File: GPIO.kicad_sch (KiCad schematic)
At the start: 34 parts, among them J11 74LS245, J9 uPD446, K15 74LS04, U1 74LS245, U2 74LS10

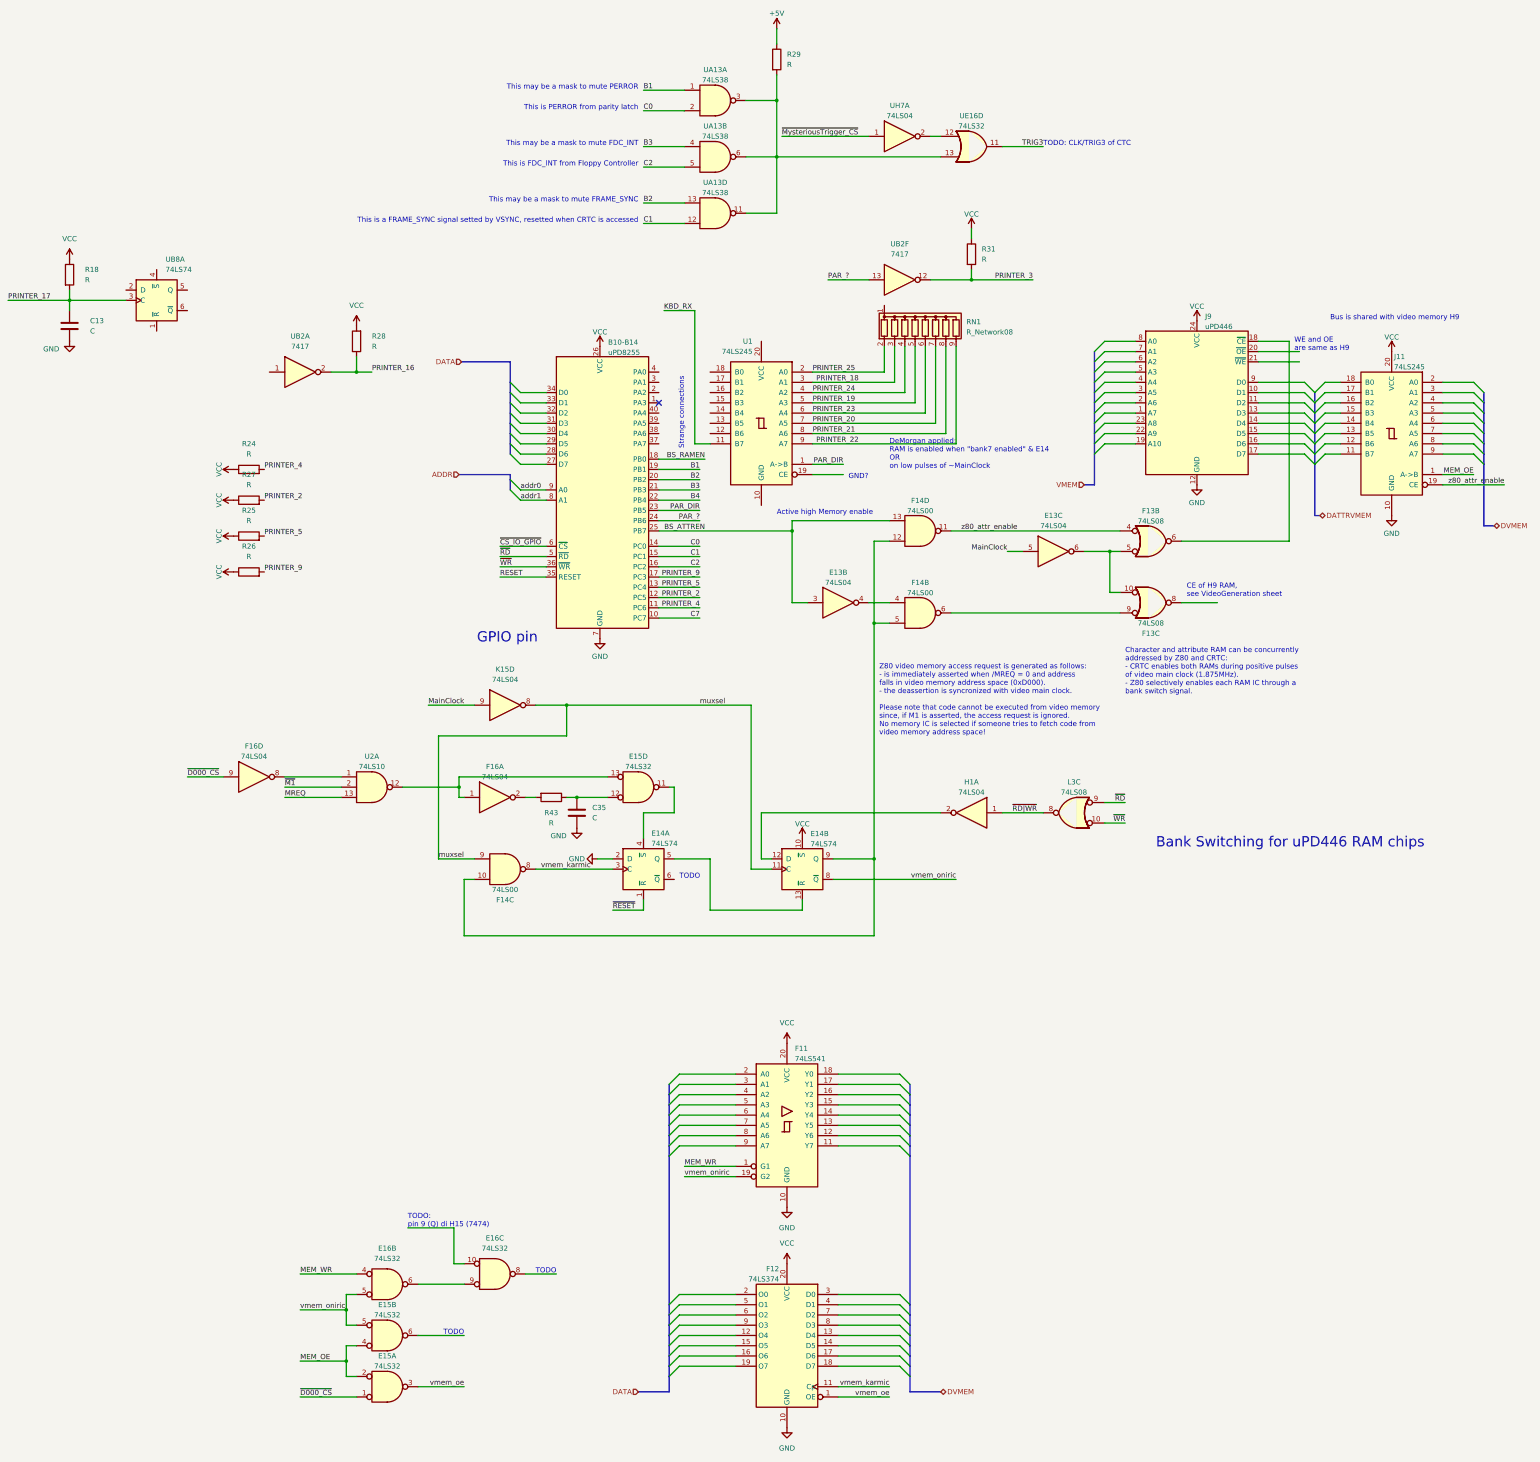
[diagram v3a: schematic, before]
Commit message: Discovered WE and OE signals for video memories, plus others
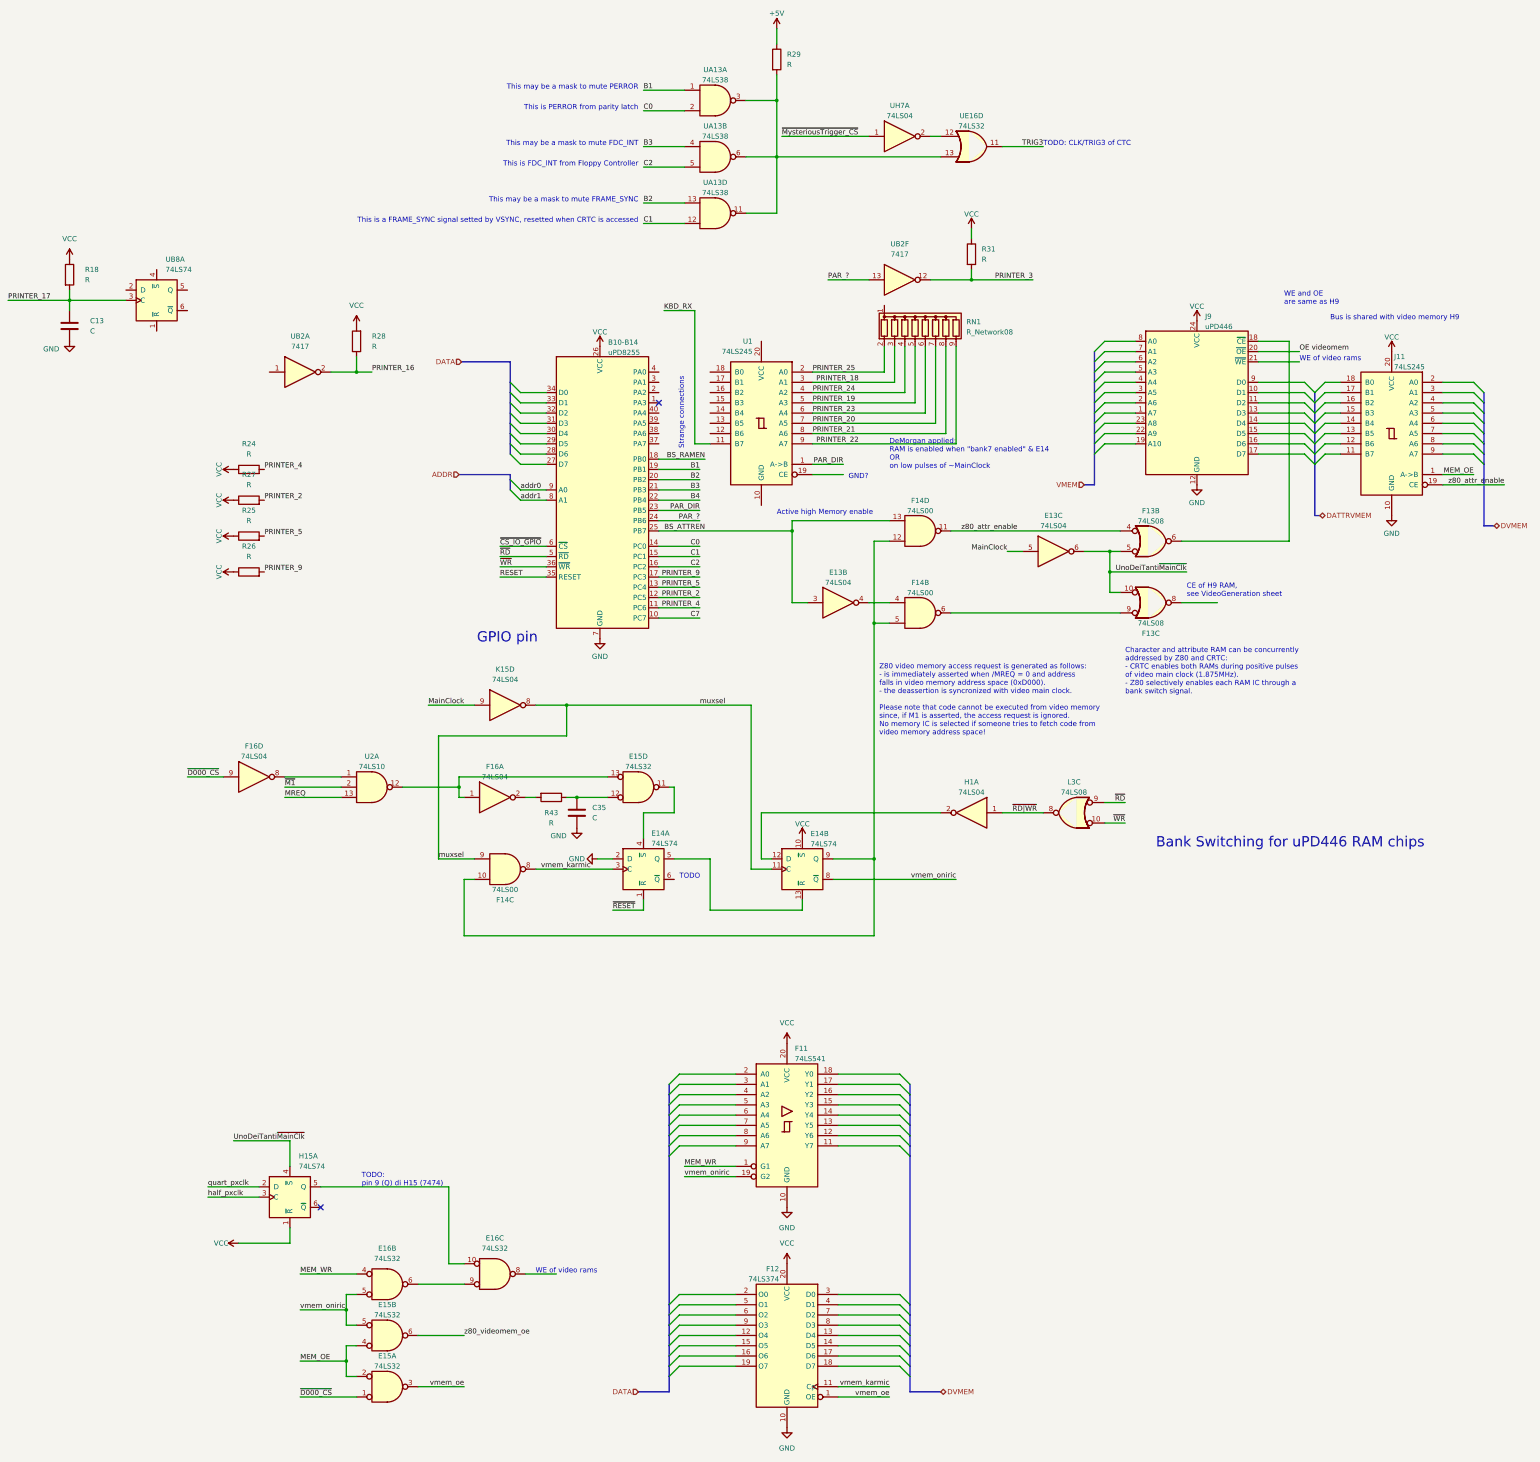
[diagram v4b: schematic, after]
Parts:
- added H15: 74LS74, symbol 74xx:74LS74
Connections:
- net VCC: now also H15.1 (~{R})
- net UnoDeiTanti~{MainClk}: now reaches E13.6, F13.10, F13.5
- net UnoDeiTanti~{MainClk}: now also H15.4 (~{S})
- net OE videomem: now reaches J9.20 (~{OE})
- net z80_videomem_oe: now reaches E15.6
- net at E16.10: now also H15.5 (Q)
- new net half_pxclk: H15.3 (C)
- new net quart_pxclk: H15.2 (D)
- no-connect marks 1 -> 2
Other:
- note added: "WE of video rams"
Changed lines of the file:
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@@
   (junction (at 49.53 147.32) (diameter 0) (color 0 0 0 0)
   )
+  (junction (at 181.61 91.44) (diameter 0) (color 0 0 0 0)
+  )
   (junction (at 20.32 144.78) (diameter 0) (color 0 0 0 0)
   )
@@
   )
   (no_connect (at 69.85 49.53))
+  (no_connect (at -13.97 248.92))
   (bus_entry (at 271.78 62.23) (size 2.54 2.54)
     (stroke (width 0) (type default))
@@
     (stroke (width 0) (type default))
   )
+  (wire (pts (xy -21.59 254) (xy -21.59 257.81))
+    (stroke (width 0) (type default))
+  )
   (wire (pts (xy 218.44 34.29) (xy 226.06 34.29))
     (stroke (width 0) (type default))
@@
     (stroke (width 0) (type default))
   )
-  (wire (pts (xy 19.05 262.89) (xy 19.05 254))
+  (wire (pts (xy 17.78 262.89) (xy 17.78 243.84))
     (stroke (width 0) (type default))
   )
@@
     (stroke (width 0) (type default))
   )
+  (wire (pts (xy -41.91 243.84) (xy -29.21 243.84))
+    (stroke (width 0) (type default))
+  )
   (wire (pts (xy 74.93 270.51) (xy 88.9 270.51))
     (stroke (width 0) (type default))
@@
     (stroke (width 0) (type default))
   )
+  (wire (pts (xy 200.66 91.44) (xy 181.61 91.44))
+    (stroke (width 0) (type default))
+  )
   (bus (pts (xy 274.32 62.23) (xy 274.32 64.77))
     (stroke (width 0) (type default))
@@
     (stroke (width 0) (type default))
   )
-  (wire (pts (xy 21.59 262.89) (xy 19.05 262.89))
+  (wire (pts (xy 17.78 262.89) (xy 21.59 262.89))
     (stroke (width 0) (type default))
   )
@@
     (stroke (width 0) (type default))
   )
+  (wire (pts (xy -13.97 243.84) (xy 17.78 243.84))
+    (stroke (width 0) (type default))
+  )
   (bus (pts (xy 177.8 57.15) (xy 177.8 59.69))
     (stroke (width 0) (type default))
@@
     (stroke (width 0) (type default))
   )
+  (wire (pts (xy 181.61 91.44) (xy 181.61 96.52))
+    (stroke (width 0) (type default))
+  )
   (wire (pts (xy 97.79 162.56) (xy 95.25 162.56))
     (stroke (width 0) (type default))
@@
     (stroke (width 0) (type default))
   )
+  (wire (pts (xy -34.29 257.81) (xy -21.59 257.81))
+    (stroke (width 0) (type default))
+  )
   (wire (pts (xy 114.3 231.14) (xy 129.54 231.14))
     (stroke (width 0) (type default))
@@
     (stroke (width 0) (type default))
   )
+  (wire (pts (xy -35.56 232.41) (xy -21.59 232.41))
+    (stroke (width 0) (type default))
+  )
   (wire (pts (xy 121.92 19.05) (xy 111.76 19.05))
     (stroke (width 0) (type default))
@@
     (stroke (width 0) (type default))
   )
-  (wire (pts (xy 181.61 86.36) (xy 181.61 96.52))
+  (wire (pts (xy 181.61 86.36) (xy 181.61 91.44))
     (stroke (width 0) (type default))
   )
@@
     (stroke (width 0) (type default))
   )
-  (wire (pts (xy 7.62 254) (xy 19.05 254))
-    (stroke (width 0) (type default))
-  )
   (bus (pts (xy 274.32 80.01) (xy 276.86 80.01))
     (stroke (width 0) (type default))
@@
     (stroke (width 0) (type default))
   )
+  (wire (pts (xy -41.91 246.38) (xy -29.21 246.38))
+    (stroke (width 0) (type default))
+  )
+  (wire (pts (xy -21.59 238.76) (xy -21.59 232.41))
+    (stroke (width 0) (type default))
+  )
   (wire (pts (xy 69.85 97.79) (xy 80.01 97.79))
     (stroke (width 0) (type default))
@@
     (effects (font (size 2.54 2.54)) (justify left bottom))
   )
-  (text "WE and OE\nare same as H9" (at 227.33 36.83 0)
+  (text "WE and OE\nare same as H9" (at 224.79 25.4 0)
     (effects (font (size 1.27 1.27)) (justify left bottom))
   )
@@
     (effects (font (size 1.27 1.27)) (justify left bottom))
   )
-  (text "TODO" (at 44.45 265.43 0)
+  (text "WE of video rams" (at 54.61 265.43 0)
     (effects (font (size 1.27 1.27)) (justify right bottom))
   )
+  (text "WE of video rams" (at 228.6 39.37 0)
+    (effects (font (size 1.27 1.27)) (justify left bottom))
+  )
   (text "Character and attribute RAM can be concurrently\naddressed by Z80 and CRTC:\n- CRTC enables both RAMs during positive pulses\nof video main clock (1.875MHz).\n- Z80 selectively enables each RAM IC through a\nbank switch signal."
     (at 185.42 121.92 0)
@@
     (effects (font (size 1.27 1.27)) (justify right bottom))
   )
-  (text "TODO:\npin 9 (Q) di H15 (7474)" (at 7.62 254 0)
+  (text "TODO:\npin 9 (Q) di H15 (7474)" (at -3.81 243.84 0)
     (effects (font (size 1.27 1.27)) (justify left bottom))
   )
@@
     (effects (font (size 1.27 1.27)) (justify left bottom))
   )
-  (text "TODO" (at 21.59 280.67 0)
-    (effects (font (size 1.27 1.27)) (justify right bottom))
-  )
   (text "Z80 video memory access request is generated as follows:\n- is immediately asserted when /MREQ = 0 and address\nfalls in video memory address space (0xD000).\n- the deassertion is syncronized with video main clock.\n\nPlease note that code cannot be executed from video memory\nsince, if M1 is asserted, the access request is ignored.\nNo memory IC is selected if someone tries to fetch code from\nvideo memory address space!"
     (at 124.46 132.08 0)
@@
     (effects (font (size 1.27 1.27)) (justify right bottom))
   )
+  (label "half_pxclk" (at -41.91 246.38 0) (fields_autoplaced)
+    (effects (font (size 1.27 1.27)) (justify left bottom))
+  )
   (label "MEM_OE" (at -19.05 287.02 0) (fields_autoplaced)
     (effects (font (size 1.27 1.27)) (justify left bottom))
@@
     (effects (font (size 1.27 1.27)) (justify left bottom))
   )
+  (label "quart_pxclk" (at -41.91 243.84 0) (fields_autoplaced)
+    (effects (font (size 1.27 1.27)) (justify left bottom))
+  )
   (label "PRINTER_16" (at -1.27 41.91 0) (fields_autoplaced)
     (effects (font (size 1.27 1.27)) (justify left bottom))
@@
     (effects (font (size 1.27 1.27)) (justify left bottom))
   )
+  (label "UnoDeiTanti~{MainClk}" (at 200.66 91.44 180) (fields_autoplaced)
+    (effects (font (size 1.27 1.27)) (justify right bottom))
+  )
   (label "PAR_DIR" (at 115.57 64.77 180) (fields_autoplaced)
     (effects (font (size 1.27 1.27)) (justify right bottom))
@@
     (effects (font (size 1.27 1.27)) (justify left bottom))
   )
+  (label "UnoDeiTanti~{MainClk}" (at -35.56 232.41 0) (fields_autoplaced)
+    (effects (font (size 1.27 1.27)) (justify left bottom))
+  )
   (label "PRINTER_18" (at 119.38 44.45 180) (fields_autoplaced)
     (effects (font (size 1.27 1.27)) (justify right bottom))
@@
     (effects (font (size 1.27 1.27)) (justify right bottom))
   )
+  (label "z80_videomem_oe" (at 21.59 280.67 0) (fields_autoplaced)
+    (effects (font (size 1.27 1.27)) (justify left bottom))
+  )
   (label "~{M1}" (at -22.86 144.78 0) (fields_autoplaced)
     (effects (font (size 1.27 1.27)) (justify left bottom))
@@
     (effects (font (size 1.27 1.27)) (justify right bottom))
   )
+  (label "OE videomem" (at 228.6 36.83 0) (fields_autoplaced)
+    (effects (font (size 1.27 1.27)) (justify left bottom))
+  )
   (label "PRINTER_4" (at -27.94 66.04 0) (fields_autoplaced)
     (effects (font (size 1.27 1.27)) (justify left bottom))
@@
     )
   )
+  (symbol (lib_id "power:VCC") (at -34.29 257.81 90) (unit 1)
+    (in_bom yes) (on_board yes) (dnp no) (fields_autoplaced)
+    (property "Reference" "#PWR0115" (at -30.48 257.81 0)
+      (effects (font (size 1.27 1.27)) hide)
+    )
+    (property "Value" "VCC" (at -36.83 257.81 90)
+      (effects (font (size 1.27 1.27)) (justify left))
+    )
+    (property "Footprint" "" (at -34.29 257.81 0)
+      (effects (font (size 1.27 1.27)) hide)
+    )
+    (property "Datasheet" "" (at -34.29 257.81 0)
+      (effects (font (size 1.27 1.27)) hide)
+    )
+    (pin "1")
+    (instances
+      (project "ceda"
+        (path "/12a6dbe3-008d-4c5b-88f6-9f1c816060be/23c42ab9-740a-4e84-88f1-9f74965e7273"
+          (reference "#PWR0115") (unit 1)
+        )
+      )
+    )
+  )
   (symbol (lib_id "Device:C") (at -76.2 30.48 0) (unit 1)
     (in_bom yes) (on_board yes) (dnp no) (fields_autoplaced)
@@
         )
       )
+    )
+  )
+  (symbol (lib_id "74xx:74LS74") (at -21.59 246.38 0) (unit 1)
+    (in_bom yes) (on_board yes) (dnp no) (fields_autoplaced)
+    (property "Reference" "H15" (at -19.3959 236.22 0)
+      (effects (font (size 1.27 1.27)) (justify left))
+    )
+    (property "Value" "74LS74" (at -19.3959 238.76 0)
+      (effects (font (size 1.27 1.27)) (justify left))
+    )
+    (property "Footprint" "" (at -21.59 246.38 0)
+      (effects (font (size 1.27 1.27)) hide)
+    )
+    (property "Datasheet" "74xx/74hc_hct74.pdf" (at -21.59 246.38 0)
+      (effects (font (size 1.27 1.27)) hide)
+    )
+    (pin "1")
+    (pin "2")
+    (pin "3")
+    (pin "4")
+    (pin "5")
+    (pin "6")
+    (pin "10")
+    (pin "11")
+    (pin "12")
+    (pin "13")
+    (pin "8")
+    (pin "9")
+    (pin "14")
+    (pin "7")
+    (instances
+      (project "ceda"
+        (path "/12a6dbe3-008d-4c5b-88f6-9f1c816060be/d9e42cc5-3ed8-41e5-aab1-e3ef5c13a809"
+          (reference "H15") (unit 1)
+        )
+        (path "/12a6dbe3-008d-4c5b-88f6-9f1c816060be/23c42ab9-740a-4e84-88f1-9f74965e7273"
+          (reference "UH15") (unit 2)
+        )
+      )
